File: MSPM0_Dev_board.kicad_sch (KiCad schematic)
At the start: 5 parts, among them U1 MSPM0G3507SPTR

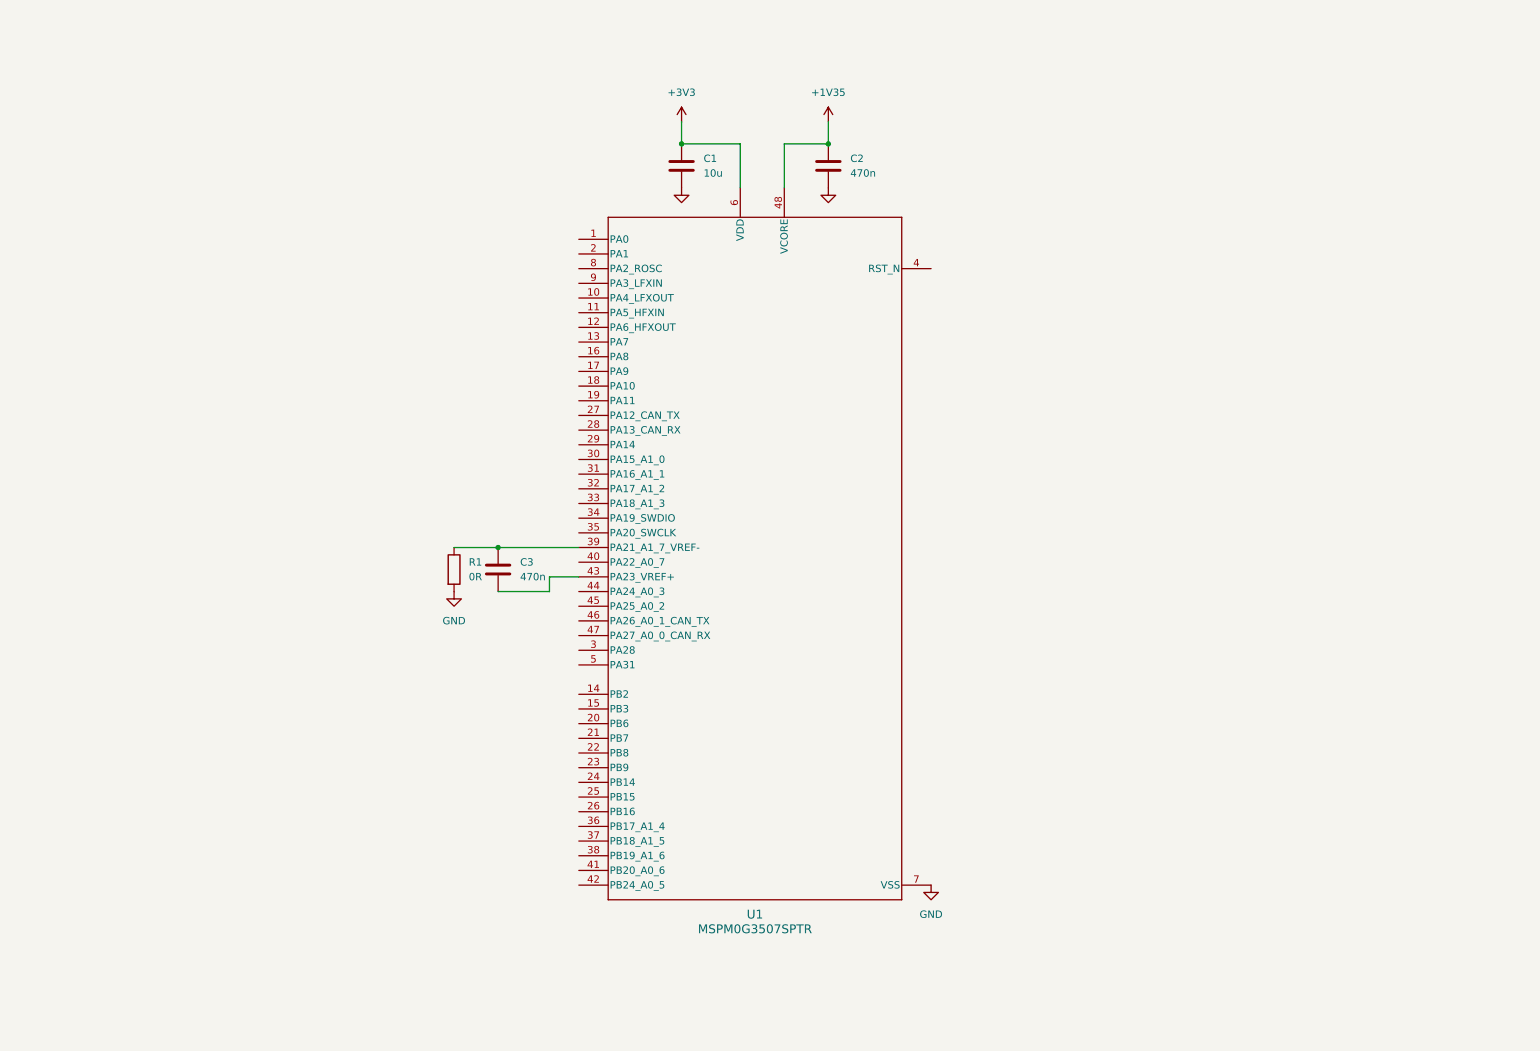
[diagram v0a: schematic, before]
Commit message: update schematic
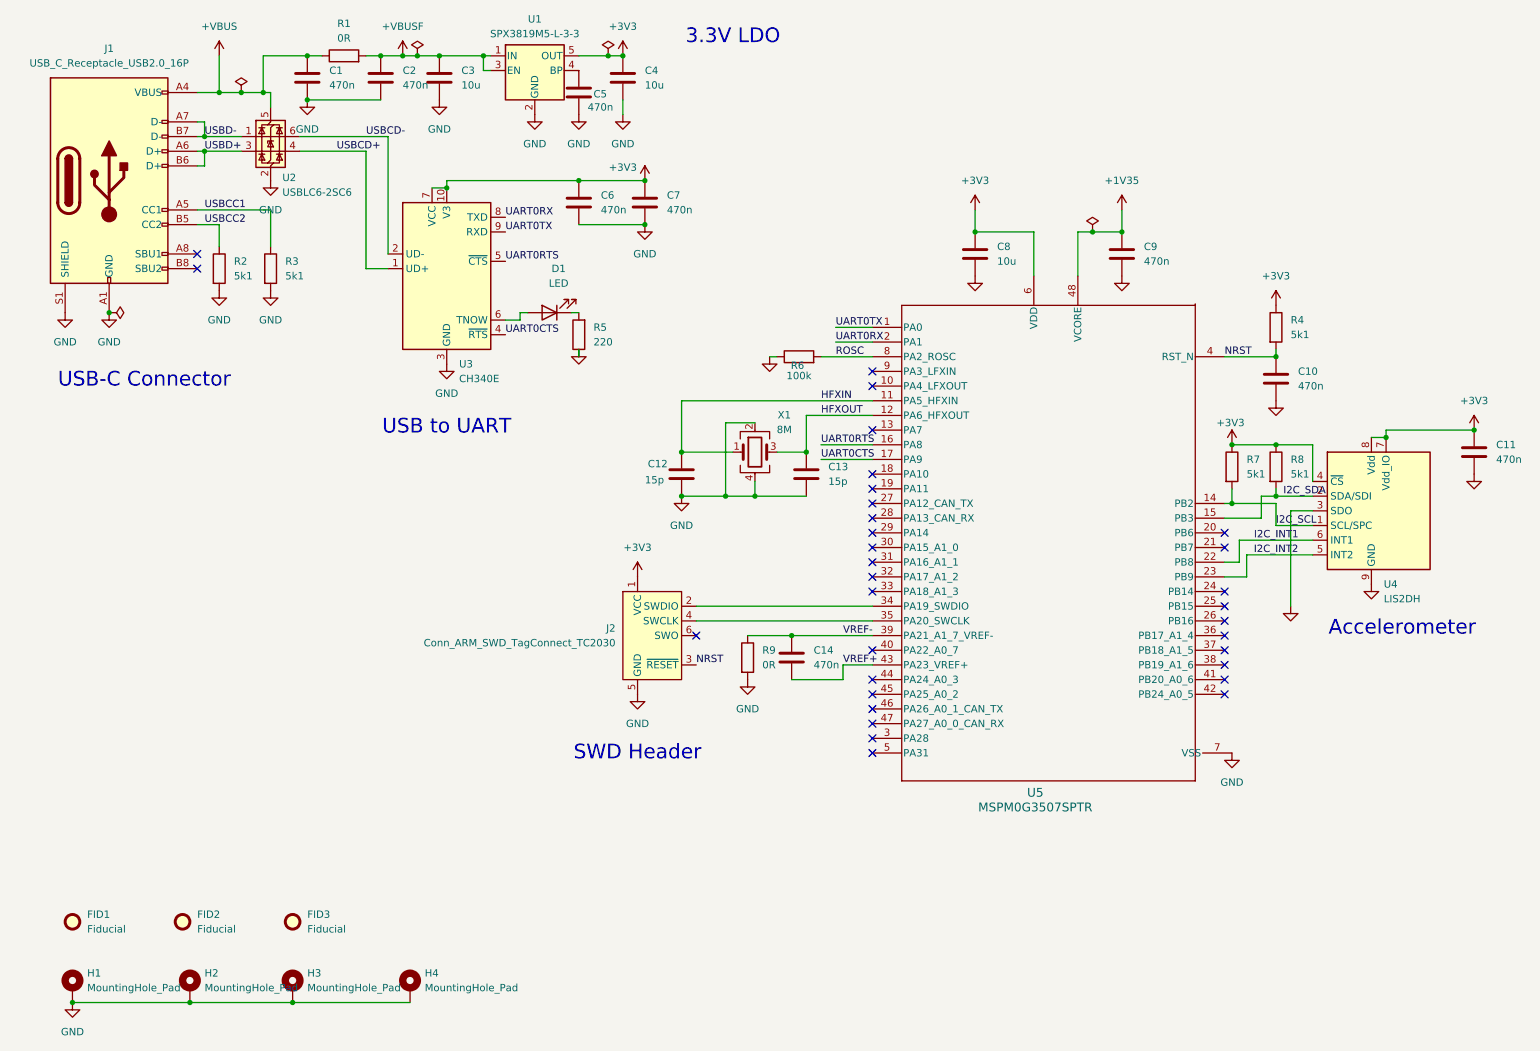
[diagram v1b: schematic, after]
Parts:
- added C1, C2, C5, C6, C7: 470n, Capacitor_SMD:C_0805_2012Metric, symbol Device:C
- added C10, C11: 470n, Capacitor_SMD:C_0603_1608Metric, symbol Device:C
- added C12, C13: 15p, Capacitor_SMD:C_0603_1608Metric, symbol Device:C
- added C3, C4: 10u, Capacitor_SMD:C_0805_2012Metric, symbol Device:C
- added D1: LED, symbol Device:LED
- added FID1, FID2, FID3: Fiducial, Fiducial:Fiducial_1mm_Mask2mm, symbol Mechanical:Fiducial
- added H1, H2, H3, H4: MountingHole_Pad, MountingHole:MountingHole_3.2mm_M3_DIN965_Pad, symbol Mechanical:MountingHole_Pad
- added J1: USB_C_Receptacle_USB2.0_16P, Connector_USB:USB_C_Receptacle_Amphenol_12401610E4-2A, symbol Connector:USB_C_Receptacle_USB2.0_16P
- added J2: Conn_ARM_SWD_TagConnect_TC2030, Connector:Tag-Connect_TC2030-IDC-FP_2x03_P1.27mm_Vertical, symbol Connector:Conn_ARM_SWD_TagConnect_TC2030
- added R1: 0R, symbol Device:R
- added R2, R3, R4, R7, R8: 5k1, symbol Device:R
- added R5: 220, symbol Device:R
- added R6: 100k, symbol Device:R
- added U1: SPX3819M5-L-3-3, Package_TO_SOT_SMD:SOT-23-5, symbol Regulator_Linear:SPX3819M5-L-3-3
- added U2: USBLC6-2SC6, Package_TO_SOT_SMD:SOT-23-6, symbol Power_Protection:USBLC6-2SC6
- added U3: CH340E, Package_SO:MSOP-10_3x3mm_P0.5mm, symbol Interface_USB:CH340E
- added U4: LIS2DH, Package_LGA:LGA-14_2x2mm_P0.35mm_LayoutBorder3x4y, symbol Sensor_Motion:LIS2DH
- added X1: 8M, Crystal:Crystal_SMD_3225-4Pin_3.2x2.5mm_HandSoldering, symbol Device:Crystal_GND24
- renumbered C3 to C14, C1 to C8, C2 to C9, R1 to R9, U1 to U5
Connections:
- net +3V3: now also C11.1, C4.1, C6.1, C7.1, J2.1 (VCC), R4.1, R7.1, R8.1, U1.5 (OUT), U3.10 (V3), U3.7 (VCC), U4.4 (~{CS}), U4.7 (Vdd_IO), U4.8 (Vdd)
- net GND: now also C1.2, C10.2, C11.2, C12.2, C13.2, C2.2, C3.2, C4.2, C5.2, C6.2, C7.2, H1.1, H2.1, H3.1, H4.1, J1.A1 (GND), J1.A12 (GND), J1.B1 (GND), J1.B12 (GND), J1.S1 (SHIELD), J2.5 (GND), R2.2, R3.2, R5.1, R6.1, U1.2 (GND), U2.2 (GND), U3.3 (GND), U4.10 (GND), U4.11 (GND), U4.12 (GND), U4.13 (GND), U4.14 (GND), U4.3 (SDO), U4.9 (GND), X1.2, X1.4
- net UART0TX: now reaches U5.1 (PA0)
- net UART0TX: now also U3.9 (RXD)
- net HFXIN: now reaches U5.11 (PA5_HFXIN)
- net HFXIN: now also C12.1, X1.1
- net HFXOUT: now reaches U5.12 (PA6_HFXOUT)
- net HFXOUT: now also C13.1, X1.3
- net I2C_SCL: now reaches U5.14 (PB2)
- net I2C_SCL: now also R7.2, U4.1 (SCL/SPC)
- net I2C_SDA: now reaches U5.15 (PB3)
- net I2C_SDA: now also R8.2, U4.2 (SDA/SDI)
- net UART0RTS: now reaches U5.16 (PA8)
- net UART0RTS: now also U3.5 (~{CTS})
- net UART0CTS: now reaches U5.17 (PA9)
- net UART0CTS: now also U3.4 (~{RTS})
- net UART0RX: now reaches U5.2 (PA1)
- net UART0RX: now also U3.8 (TXD)
- net I2C_INT1: now reaches U5.22 (PB8)
- net I2C_INT1: now also U4.6 (INT1)
- net I2C_INT2: now reaches U5.23 (PB9)
- net I2C_INT2: now also U4.5 (INT2)
- net at U5.34 (PA19_SWDIO): now also J2.2 (SWDIO)
- net at U5.35 (PA20_SWCLK): now also J2.4 (SWCLK)
- net VREF-: now reaches C14.1, R9.1, U5.39 (PA21_A1_7_VREF-)
- net NRST: now reaches U5.4 (RST_N)
- net NRST: now also C10.1, J2.3 (~{RESET}), R4.2
- net VREF+: now reaches C14.2, U5.43 (PA23_VREF+)
- net ROSC: now reaches U5.8 (PA2_ROSC)
- net ROSC: now also R6.2
- new net: D1.2 (A), U3.6 (TNOW)
- new net: C5.1, U1.4 (BP)
- new net: D1.1 (K), R5.2
- new net +VBUS: C1.1, J1.A4 (VBUS), J1.A9 (VBUS), J1.B4 (VBUS), J1.B9 (VBUS), R1.1, U2.5 (VBUS)
- new net +VBUSF: C2.1, C3.1, R1.2, U1.1 (IN), U1.3 (EN)
- new net USBCC1: J1.A5 (CC1), R3.1
- new net USBCC2: J1.B5 (CC2), R2.1
- new net USBCD+: U2.4 (I/O2), U3.1 (UD+)
- new net USBCD-: U2.6 (I/O1), U3.2 (UD-)
- new net USBD+: J1.A6 (D+), J1.B6 (D+), U2.3 (I/O2)
- new net USBD-: J1.A7 (D-), J1.B7 (D-), U2.1 (I/O1)
- no-connect marks 0 -> 32
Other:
- note added: "3.3V LDO"
- note added: "Accelerometer"
- note added: "SWD Header"
- note added: "USB to UART"
- note added: "USB-C Connector"
- moved on the sheet: C14, C8, C9, R9, U5
